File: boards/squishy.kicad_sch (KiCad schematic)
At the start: 54 parts, among them J1 USB_B_Micro, J2 Conn_02x26_Top_Bottom, J3 Conn_02x05_Odd_Even, J4 Conn_01x04, Q1 Q_PMOS_DGS, U1 W25N01GVZEIG, U2 ICE40HX8K-BG121, U3 USB3318, X1 48MHz, X2 16MHz

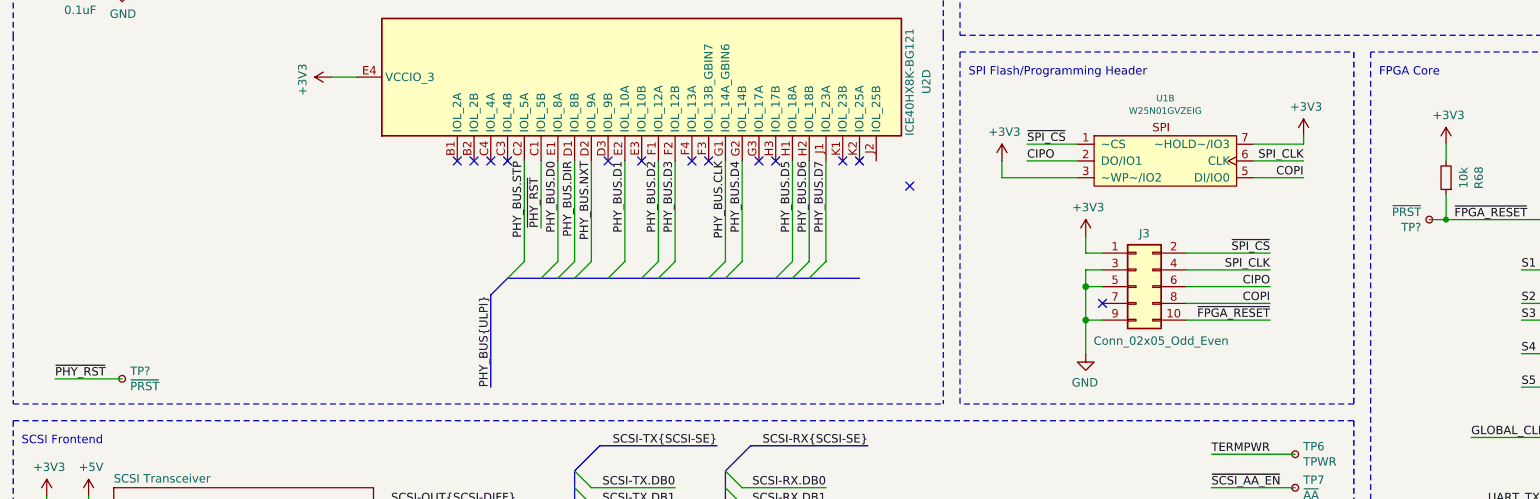
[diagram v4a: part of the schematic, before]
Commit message: hardware: fixed a blip in the scsi wiggles, added ESD protection to the USB line because i got bullied into doing so
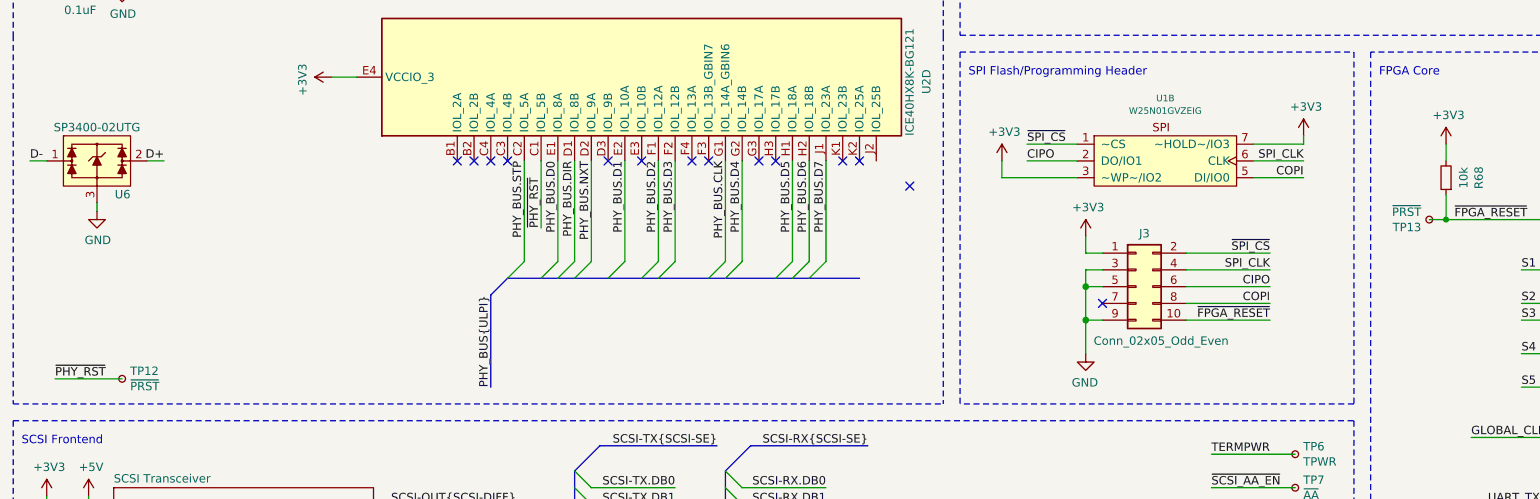
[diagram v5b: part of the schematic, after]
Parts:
- added U6: SP3400-02UTG, rhais_package-qfn:UDFN-6L, symbol DX-MON-NG:SP3400-02UTG
- gave numbers to parts that had none: 2
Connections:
- net D+: now also U6.2 (IO2), U6.5 (NC)
- net D-: now also U6.1 (IO1), U6.6 (NC)
- net GND: now also U6.3 (GND), U6.4 (GND)
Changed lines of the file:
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@@
     (stroke (width 0) (type solid) (color 0 0 0 0))
   )
+  (wire (pts (xy 19.05 88.9) (xy 16.51 88.9))
+    (stroke (width 0) (type solid) (color 0 0 0 0))
+  )
   (wire (pts (xy 19.05 143.51) (xy 19.05 139.7))
     (stroke (width 0) (type solid) (color 0 0 0 0))
@@
     (stroke (width 0) (type solid) (color 0 0 0 0))
   )
+  (wire (pts (xy 26.67 96.52) (xy 26.67 95.25))
+    (stroke (width 0) (type solid) (color 0 0 0 0))
+  )
   (wire (pts (xy 26.67 252.73) (xy 26.67 250.19))
     (stroke (width 0) (type solid) (color 0 0 0 0))
@@
     (stroke (width 0) (type solid) (color 0 0 0 0))
   )
+  (wire (pts (xy 34.29 88.9) (xy 36.83 88.9))
+    (stroke (width 0) (type solid) (color 0 0 0 0))
+  )
   (wire (pts (xy 34.29 262.89) (xy 34.29 260.35))
     (stroke (width 0) (type solid) (color 0 0 0 0))
@@
     (effects (font (size 1.27 1.27)) (justify left bottom))
   )
+  (label "D-" (at 16.51 88.9 0)
+    (effects (font (size 1.27 1.27)) (justify left bottom))
+  )
   (label "~{SCSI_AA_EN}" (at 16.51 152.4 0)
     (effects (font (size 1.27 1.27)) (justify left bottom))
@@
     (effects (font (size 1.27 1.27)) (justify right bottom))
   )
+  (label "D+" (at 36.83 88.9 180)
+    (effects (font (size 1.27 1.27)) (justify right bottom))
+  )
   (label "~{TP_EN}" (at 41.91 270.51 180)
     (effects (font (size 1.27 1.27)) (justify right bottom))
@@
   (symbol (lib_id "Connector:TestPoint_Small") (at 30.48 121.92 0) (unit 1)
     (in_bom yes) (on_board yes)
-    (property "Reference" "TP?" (id 0) (at 31.6992 120.7516 0)
+    (property "Reference" "TP12" (id 0) (at 31.6992 120.7516 0)
       (effects (font (size 1.27 1.27)) (justify left))
     )
@@
   (symbol (lib_id "Connector:TestPoint_Small") (at 228.6 97.79 180) (unit 1)
     (in_bom yes) (on_board yes)
-    (property "Reference" "TP?" (id 0) (at 227.3808 98.9584 0)
+    (property "Reference" "TP13" (id 0) (at 227.3808 98.9584 0)
       (effects (font (size 1.27 1.27)) (justify left))
     )
@@
     (pin "1")
   )
+  (symbol (lib_id "power:GND") (at 26.67 96.52 0) (unit 1)
+    (in_bom yes) (on_board yes)
+    (property "Reference" "#PWR0239" (id 0) (at 26.67 102.87 0)
+      (effects (font (size 1.27 1.27)) hide)
+    )
+    (property "Value" "GND" (id 1) (at 26.797 100.9142 0))
+    (property "Footprint" "" (id 2) (at 26.67 96.52 0)
+      (effects (font (size 1.27 1.27)) hide)
+    )
+    (property "Datasheet" "" (id 3) (at 26.67 96.52 0)
+      (effects (font (size 1.27 1.27)) hide)
+    )
+    (pin "1")
+  )
   (symbol (lib_id "power:GND") (at 30.48 62.23 0) (unit 1)
     (in_bom yes) (on_board yes)
@@
     (pin "3")
   )
+  (symbol (lib_id "DX-MON-NG:SP3400-02UTG") (at 26.67 88.9 0) (unit 1)
+    (in_bom yes) (on_board yes)
+    (property "Reference" "U6" (id 0) (at 31.75 93.98 0)
+      (effects (font (size 1.27 1.27)) (justify right))
+    )
+    (property "Value" "SP3400-02UTG" (id 1) (at 26.67 83.82 0))
+    (property "Footprint" "rhais_package-qfn:UDFN-6L" (id 2) (at 26.67 107.95 0)
+      (effects (font (size 1.27 1.27)) hide)
+    )
+    (property "Datasheet" "https://www.littelfuse.com/~/media/electronics/datasheets/tvs_diode_arrays/littelfuse_tvs_diode_array_sp3400_datasheet.pdf" (id 3) (at 26.67 110.49 0)
+      (effects (font (size 1.27 1.27)) hide)
+    )
+    (property "MFR" "Littlefuse" (id 4) (at 26.67 102.87 0)
+      (effects (font (size 1.27 1.27)) hide)
+    )
+    (property "MPN" "SP3400-02UTG" (id 5) (at 26.67 105.41 0)
+      (effects (font (size 1.27 1.27)) hide)
+    )
+    (pin "1")
+    (pin "2")
+    (pin "3")
+    (pin "4")
+    (pin "5")
+    (pin "6")
+  )
   (symbol (lib_id "Connector_Generic:Conn_02x05_Odd_Even") (at 184.15 107.95 0) (unit 1)
     (in_bom yes) (on_board yes)
@@
       (reference "#PWR0238") (unit 1) (value "+3V3") (footprint "")
     )
+    (path "/cf219933-5b49-4a2e-a9bc-163e88ee7173"
+      (reference "#PWR0239") (unit 1) (value "GND") (footprint "")
+    )
     (path "/00000000-0000-0000-0000-00005f0d7af1"
       (reference "C1") (unit 1) (value "0.1uF") (footprint "Capacitor_SMD:C_0603_1608Metric")
@@
     )
     (path "/80038541-effa-4287-8941-439713c5bdb6"
-      (reference "TP?") (unit 1) (value "~{PRST}") (footprint "TestPoint:TestPoint_Pad_D1.0mm")
+      (reference "TP12") (unit 1) (value "~{PRST}") (footprint "TestPoint:TestPoint_Pad_D1.0mm")
     )
     (path "/c65a6615-4b3e-4786-acd8-db1b7e11db3e"
-      (reference "TP?") (unit 1) (value "~{PRST}") (footprint "TestPoint:TestPoint_Pad_D1.0mm")
+      (reference "TP13") (unit 1) (value "~{PRST}") (footprint "TestPoint:TestPoint_Pad_D1.0mm")
     )
     (path "/135fa4cc-bf68-4ed2-9d1e-cefa9ceb3983/44f7f89d-f61a-424b-8f8b-f31a10fe8aec"
@@
       (reference "U5") (unit 1) (value "LP5910-1.8DRVR") (footprint "Package_SON:WSON-6-1EP_2x2mm_P0.65mm_EP1x1.6mm_ThermalVias")
     )
+    (path "/8ebce395-10bd-4ec2-8574-da3537552890"
+      (reference "U6") (unit 1) (value "SP3400-02UTG") (footprint "rhais_package-qfn:UDFN-6L")
+    )
     (path "/135fa4cc-bf68-4ed2-9d1e-cefa9ceb3983/9c100b23-59b5-432e-b1a9-49cc58b7d14a"

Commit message: hardware: a bunch of clean up and the like
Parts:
- renumbered C4 to C1, C1 to C11, C43 to C29, C66 to C30, C67 to C32, C42 to C37, C69 to C45, C68 to C48, C3 to C52, C6 to C54, C5 to C55, C7 to C57, C2 to C60, D5 to D3, D6 to D4, D9 to D5, D10 to D6, J4 to J3, J3 to J4, R59 to R1, R1 to R10, R63 to R13, R64 to R14, R65 to R16, R66 to R17, R67 to R19, R69 to R20, R71 to R52, R68 to R53, R74 to R57, R85 to R62, R3 to R7, R4 to R72, R70 to R77, TP7 to TP10, TP9 to TP11, TP8 to TP12, TP6 to TP13, TP12 to TP6, TP13 to TP7, TP11 to TP8, TP10 to TP9, U6 to U12, U3 to U14, U2 to U19, U1 to U26, X2 to X1, X1 to X2

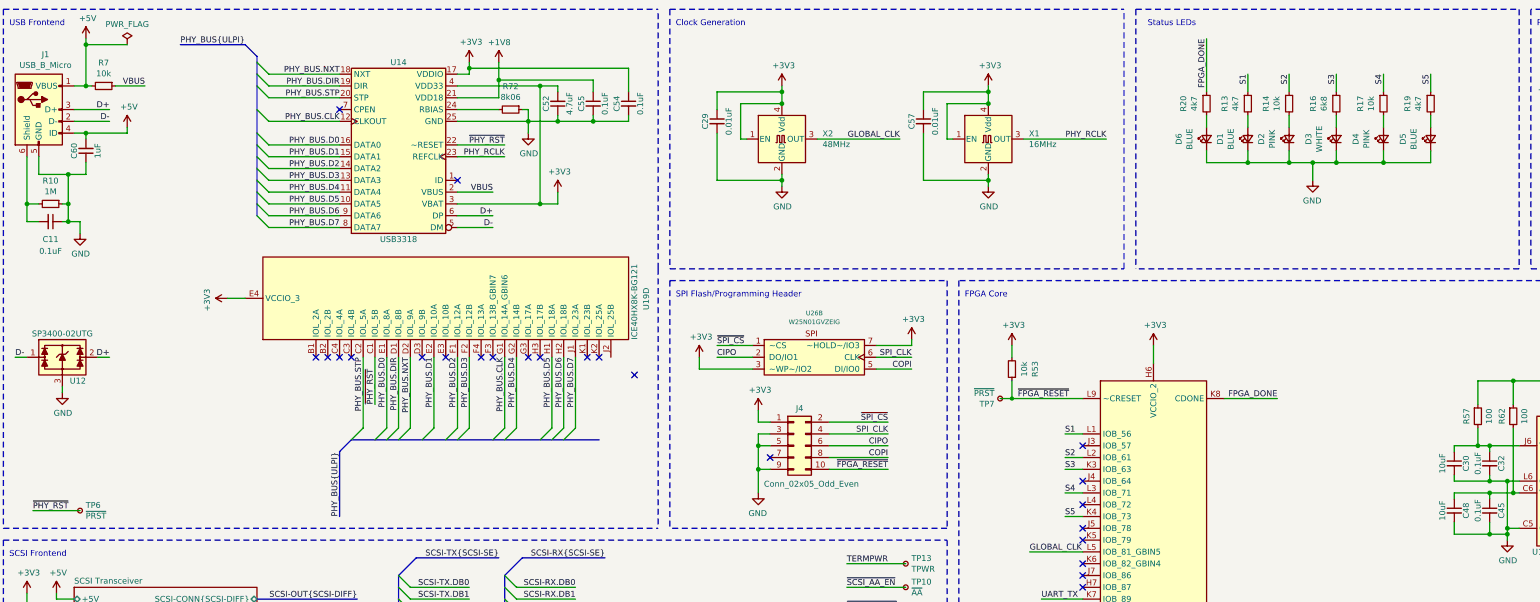
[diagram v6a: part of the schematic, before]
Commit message: hardware: ensured we got a clean bill of health from DRC and ERC
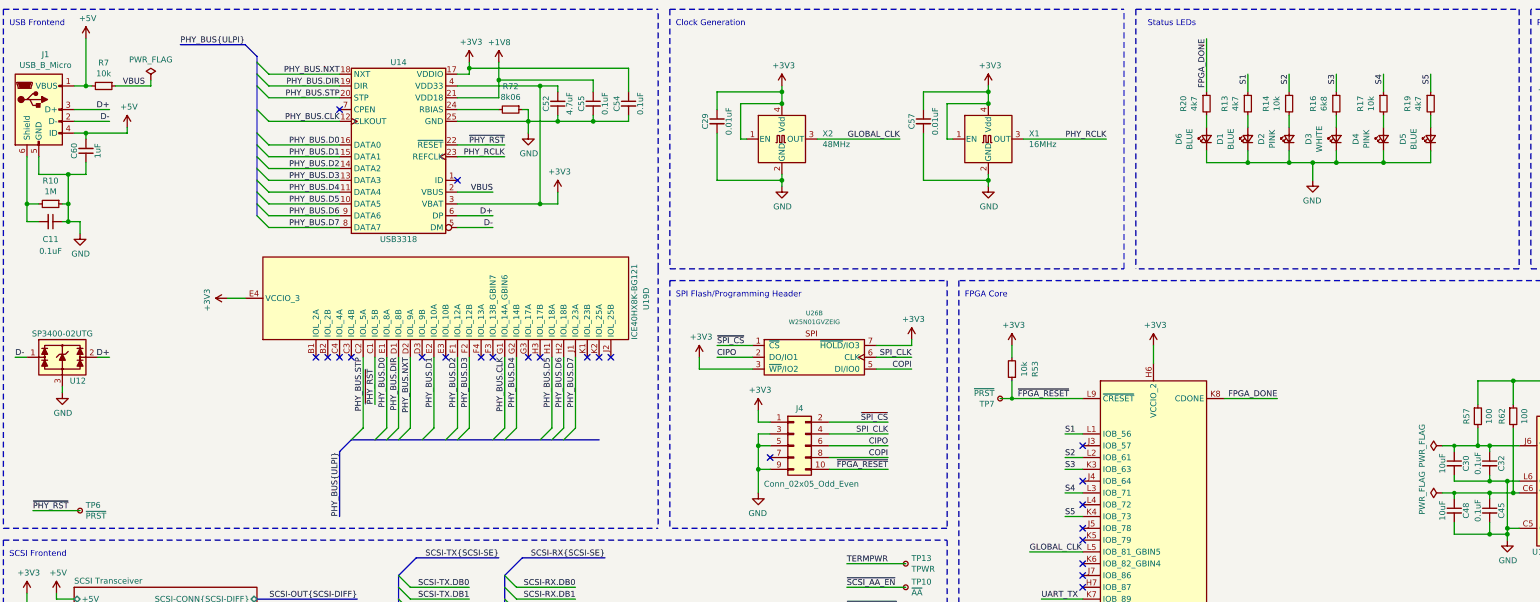
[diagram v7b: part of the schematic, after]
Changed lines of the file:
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@@
   (junction (at 27.94 55.88) (diameter 1.016) (color 0 0 0 0))
   (junction (at 27.94 59.69) (diameter 1.016) (color 0 0 0 0))
-  (junction (at 31.75 21.59) (diameter 1.016) (color 0 0 0 0))
   (junction (at 31.75 30.48) (diameter 1.016) (color 0 0 0 0))
   (junction (at 31.75 40.64) (diameter 1.016) (color 0 0 0 0))
@@
   (junction (at 300.99 46.99) (diameter 1.016) (color 0 0 0 0))
   (junction (at 311.15 46.99) (diameter 1.016) (color 0 0 0 0))
+  (junction (at 326.39 107.95) (diameter 0) (color 0 0 0 0))
+  (junction (at 326.39 118.11) (diameter 0) (color 0 0 0 0))
   (junction (at 331.47 107.95) (diameter 1.016) (color 0 0 0 0))
   (junction (at 334.01 107.95) (diameter 1.016) (color 0 0 0 0))
@@
   (no_connect (at 139.7 88.9))
   (no_connect (at 142.24 88.9))
-  (no_connect (at 149.86 92.71))
+  (no_connect (at 144.78 88.9))
   (no_connect (at 152.4 224.79))
   (no_connect (at 177.8 224.79))
@@
     (stroke (width 0) (type solid) (color 0 0 0 0))
   )
-  (wire (pts (xy 31.75 20.32) (xy 31.75 21.59))
-    (stroke (width 0) (type solid) (color 0 0 0 0))
-  )
-  (wire (pts (xy 31.75 21.59) (xy 31.75 30.48))
-    (stroke (width 0) (type solid) (color 0 0 0 0))
-  )
-  (wire (pts (xy 31.75 21.59) (xy 40.64 21.59))
+  (wire (pts (xy 31.75 20.32) (xy 31.75 30.48))
     (stroke (width 0) (type solid) (color 0 0 0 0))
   )
@@
     (stroke (width 0) (type solid) (color 0 0 0 0))
   )
-  (wire (pts (xy 38.1 30.48) (xy 44.45 30.48))
+  (wire (pts (xy 38.1 30.48) (xy 45.72 30.48))
     (stroke (width 0) (type solid) (color 0 0 0 0))
   )
@@
     (stroke (width 0) (type solid) (color 0 0 0 0))
   )
+  (wire (pts (xy 45.72 30.48) (xy 45.72 29.21))
+    (stroke (width 0) (type default) (color 0 0 0 0))
+  )
   (wire (pts (xy 49.53 194.31) (xy 68.58 194.31))
     (stroke (width 0) (type solid) (color 0 0 0 0))
@@
     (stroke (width 0) (type solid) (color 0 0 0 0))
   )
+  (wire (pts (xy 323.85 107.95) (xy 326.39 107.95))
+    (stroke (width 0) (type default) (color 0 0 0 0))
+  )
+  (wire (pts (xy 323.85 118.11) (xy 326.39 118.11))
+    (stroke (width 0) (type default) (color 0 0 0 0))
+  )
   (wire (pts (xy 326.39 107.95) (xy 331.47 107.95))
     (stroke (width 0) (type solid) (color 0 0 0 0))
@@
     (pin "1")
   )
-  (symbol (lib_id "power:PWR_FLAG") (at 40.64 21.59 0) (unit 1)
+  (symbol (lib_id "power:PWR_FLAG") (at 45.72 29.21 0) (unit 1)
     (in_bom yes) (on_board yes)
-    (property "Reference" "#FLG0101" (id 0) (at 40.64 19.685 0)
+    (property "Reference" "#FLG0105" (id 0) (at 45.72 27.305 0)
       (effects (font (size 1.27 1.27)) hide)
     )
-    (property "Value" "PWR_FLAG" (id 1) (at 40.64 17.1958 0))
-    (property "Footprint" "" (id 2) (at 40.64 21.59 0)
+    (property "Value" "PWR_FLAG" (id 1) (at 45.72 24.8158 0))
+    (property "Footprint" "" (id 2) (at 45.72 29.21 0)
       (effects (font (size 1.27 1.27)) hide)
     )
-    (property "Datasheet" "~" (id 3) (at 40.64 21.59 0)
+    (property "Datasheet" "~" (id 3) (at 45.72 29.21 0)
+      (effects (font (size 1.27 1.27)) hide)
+    )
+    (pin "1")
+  )
+  (symbol (lib_id "power:PWR_FLAG") (at 323.85 107.95 90) (unit 1)
+    (in_bom yes) (on_board yes)
+    (property "Reference" "#FLG0101" (id 0) (at 321.945 107.95 0)
+      (effects (font (size 1.27 1.27)) hide)
+    )
+    (property "Value" "PWR_FLAG" (id 1) (at 319.4558 107.95 0))
+    (property "Footprint" "" (id 2) (at 323.85 107.95 0)
+      (effects (font (size 1.27 1.27)) hide)
+    )
+    (property "Datasheet" "~" (id 3) (at 323.85 107.95 0)
+      (effects (font (size 1.27 1.27)) hide)
+    )
+    (pin "1")
+  )
+  (symbol (lib_id "power:PWR_FLAG") (at 323.85 118.11 90) (unit 1)
+    (in_bom yes) (on_board yes)
+    (property "Reference" "#FLG0102" (id 0) (at 321.945 118.11 0)
+      (effects (font (size 1.27 1.27)) hide)
+    )
+    (property "Value" "PWR_FLAG" (id 1) (at 319.4558 118.11 0))
+    (property "Footprint" "" (id 2) (at 323.85 118.11 0)
+      (effects (font (size 1.27 1.27)) hide)
+    )
+    (property "Datasheet" "~" (id 3) (at 323.85 118.11 0)
       (effects (font (size 1.27 1.27)) hide)
     )
@@
   )
   (symbol_instances
-    (path "/00000000-0000-0000-0000-00005f11005b"
+    (path "/6999bfaf-2937-4078-932b-96e83df0714b"
       (reference "#FLG0101") (unit 1) (value "PWR_FLAG") (footprint "")
     )
-    (path "/135fa4cc-bf68-4ed2-9d1e-cefa9ceb3983/22407428-afcf-4261-a2f1-75b217e58985"
+    (path "/2bcd5324-5e33-4fe9-8a27-dee860e70cbd"
       (reference "#FLG0102") (unit 1) (value "PWR_FLAG") (footprint "")
     )
-    (path "/135fa4cc-bf68-4ed2-9d1e-cefa9ceb3983/4c874c32-8491-43b8-b510-40584524022b"
-      (reference "#FLG0103") (unit 1) (value "PWR_FLAG") (footprint "")
-    )
-    (path "/135fa4cc-bf68-4ed2-9d1e-cefa9ceb3983/9e2fa65e-49bc-4eb5-82a3-cba20935d391"
-      (reference "#FLG0104") (unit 1) (value "PWR_FLAG") (footprint "")
+    (path "/0d54bdb1-3a4c-4661-a7fe-05085a30723a"
+      (reference "#FLG0105") (unit 1) (value "PWR_FLAG") (footprint "")
     )
     (path "/5a470513-af88-45a5-8151-68e0d8ddb252/a18222bc-d234-41cd-9d06-a39d2399ddf9"

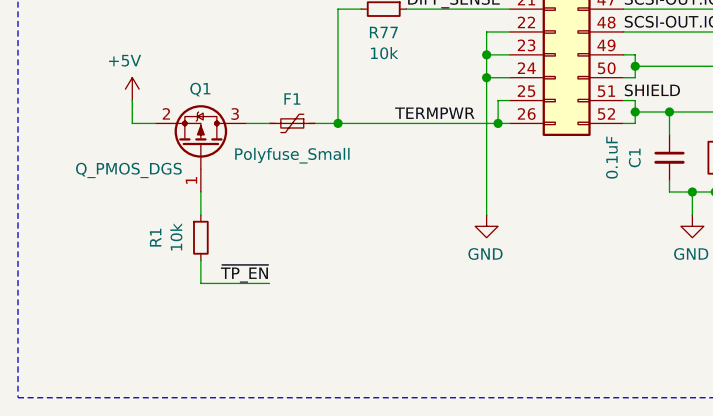
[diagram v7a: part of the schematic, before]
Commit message: hardware: fixed up some datasheets for symbols and added mounting holes
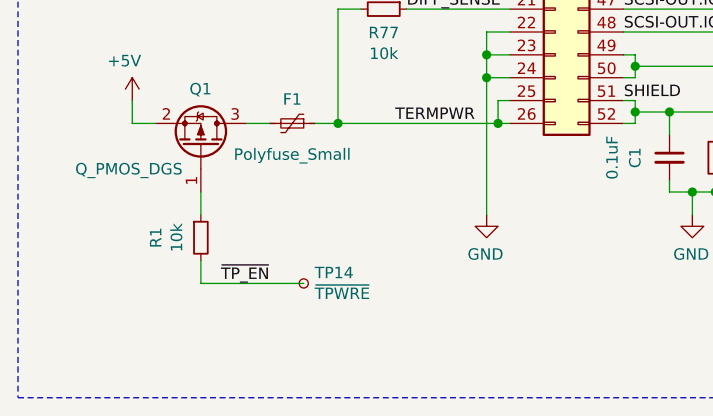
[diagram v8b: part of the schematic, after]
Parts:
- added TP14: ~{TPWRE}, TestPoint:TestPoint_Pad_D1.0mm, symbol Connector:TestPoint_Small
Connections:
- net ~{TP_EN}: now also TP14.1
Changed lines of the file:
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@@
     (stroke (width 0) (type solid) (color 0 0 0 0))
   )
-  (wire (pts (xy 34.29 270.51) (xy 41.91 270.51))
+  (wire (pts (xy 34.29 270.51) (xy 45.72 270.51))
     (stroke (width 0) (type solid) (color 0 0 0 0))
   )
@@
     (pin "1")
   )
+  (symbol (lib_id "Connector:TestPoint_Small") (at 45.72 270.51 0) (unit 1)
+    (in_bom yes) (on_board yes)
+    (property "Reference" "TP14" (id 0) (at 46.9392 269.3416 0)
+      (effects (font (size 1.27 1.27)) (justify left))
+    )
+    (property "Value" "~{TPWRE}" (id 1) (at 46.9392 271.653 0)
+      (effects (font (size 1.27 1.27)) (justify left))
+    )
+    (property "Footprint" "TestPoint:TestPoint_Pad_D1.0mm" (id 2) (at 50.8 270.51 0)
+      (effects (font (size 1.27 1.27)) hide)
+    )
+    (property "Datasheet" "~" (id 3) (at 50.8 270.51 0)
+      (effects (font (size 1.27 1.27)) hide)
+    )
+    (pin "1")
+  )
   (symbol (lib_id "Connector:TestPoint_Small") (at 208.28 133.35 0) (unit 1)
     (in_bom yes) (on_board yes)
@@
       (effects (font (size 1.27 1.27)) hide)
     )
-    (property "Datasheet" "~" (id 3) (at 34.29 255.27 0)
+    (property "Datasheet" "https://www.mouser.com/datasheet/2/427/VISH_S_A0001109972_1-2566876.pdf" (id 3) (at 34.29 255.27 0)
       (effects (font (size 1.27 1.27)) hide)
     )
@@
       (reference "G2") (unit 1) (value "Antifaschistische_Aktion") (footprint "lethalbit-graphics:Antifaschistische Aktion_600dpi")
     )
+    (path "/f0186a61-a1ec-47af-8a71-f94e7ce0e59d/4796079e-d2f0-415f-b61b-9f8efd53ee55"
+      (reference "H1") (unit 1) (value "MountingHole") (footprint "MountingHole:MountingHole_3.2mm_M3")
+    )
+    (path "/f0186a61-a1ec-47af-8a71-f94e7ce0e59d/02330466-6efc-497e-a93e-e5c6ed458b8e"
+      (reference "H2") (unit 1) (value "MountingHole") (footprint "MountingHole:MountingHole_3.2mm_M3")
+    )
+    (path "/f0186a61-a1ec-47af-8a71-f94e7ce0e59d/6384a1ab-12d7-4c05-8cd8-82c34178ee08"
+      (reference "H3") (unit 1) (value "MountingHole") (footprint "MountingHole:MountingHole_3.2mm_M3")
+    )
+    (path "/f0186a61-a1ec-47af-8a71-f94e7ce0e59d/92d55441-3aca-4558-afb6-38b34087dbcd"
+      (reference "H4") (unit 1) (value "MountingHole") (footprint "MountingHole:MountingHole_3.2mm_M3")
+    )
     (path "/00000000-0000-0000-0000-000070e3c85c"
       (reference "J1") (unit 1) (value "USB_B_Micro") (footprint "lethalbit-connectors:MICRO-USB-B-(IN_PCB)")
@@
       (reference "TP13") (unit 1) (value "TPWR") (footprint "TestPoint:TestPoint_Pad_D1.0mm")
     )
+    (path "/759194d7-42b0-4264-b119-81cc9b5a7c65"
+      (reference "TP14") (unit 1) (value "~{TPWRE}") (footprint "TestPoint:TestPoint_Pad_D1.0mm")
+    )
     (path "/5a470513-af88-45a5-8151-68e0d8ddb252/e92069a5-6c92-4eed-8047-3aa5e4866d5d"
